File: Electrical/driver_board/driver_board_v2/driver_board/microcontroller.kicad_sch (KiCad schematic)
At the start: 24 parts, among them J1 USB_C_Receptacle_USB2.0_14P, J2 Conn_01x04_Pin, SW1 SW_SPDT, SW2 SW_Push, U1 STM32F446RETx, Y1 8Mhz

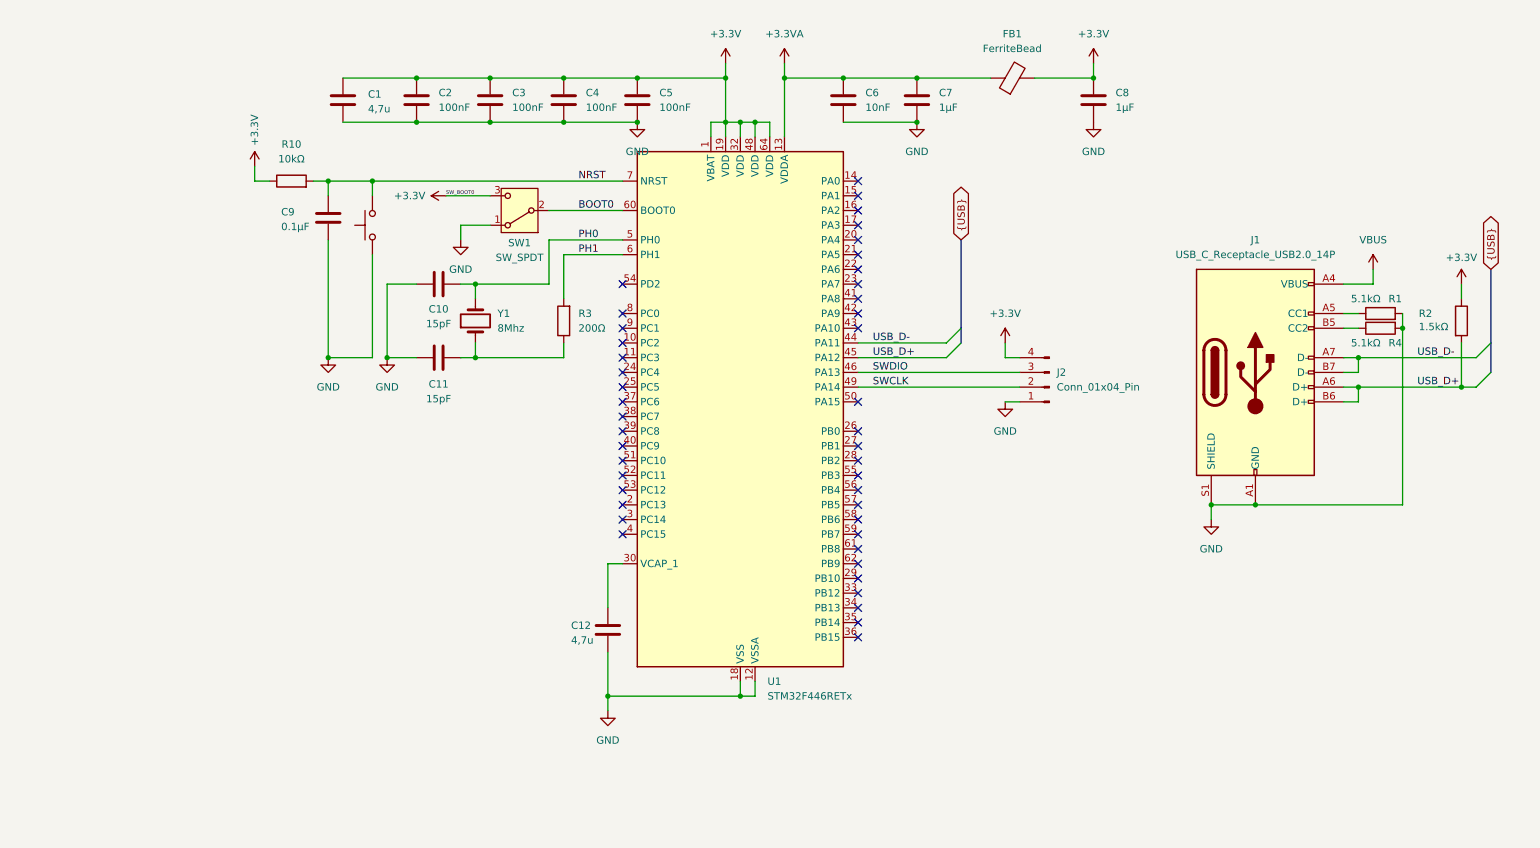
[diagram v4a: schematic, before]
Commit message: Added gripper
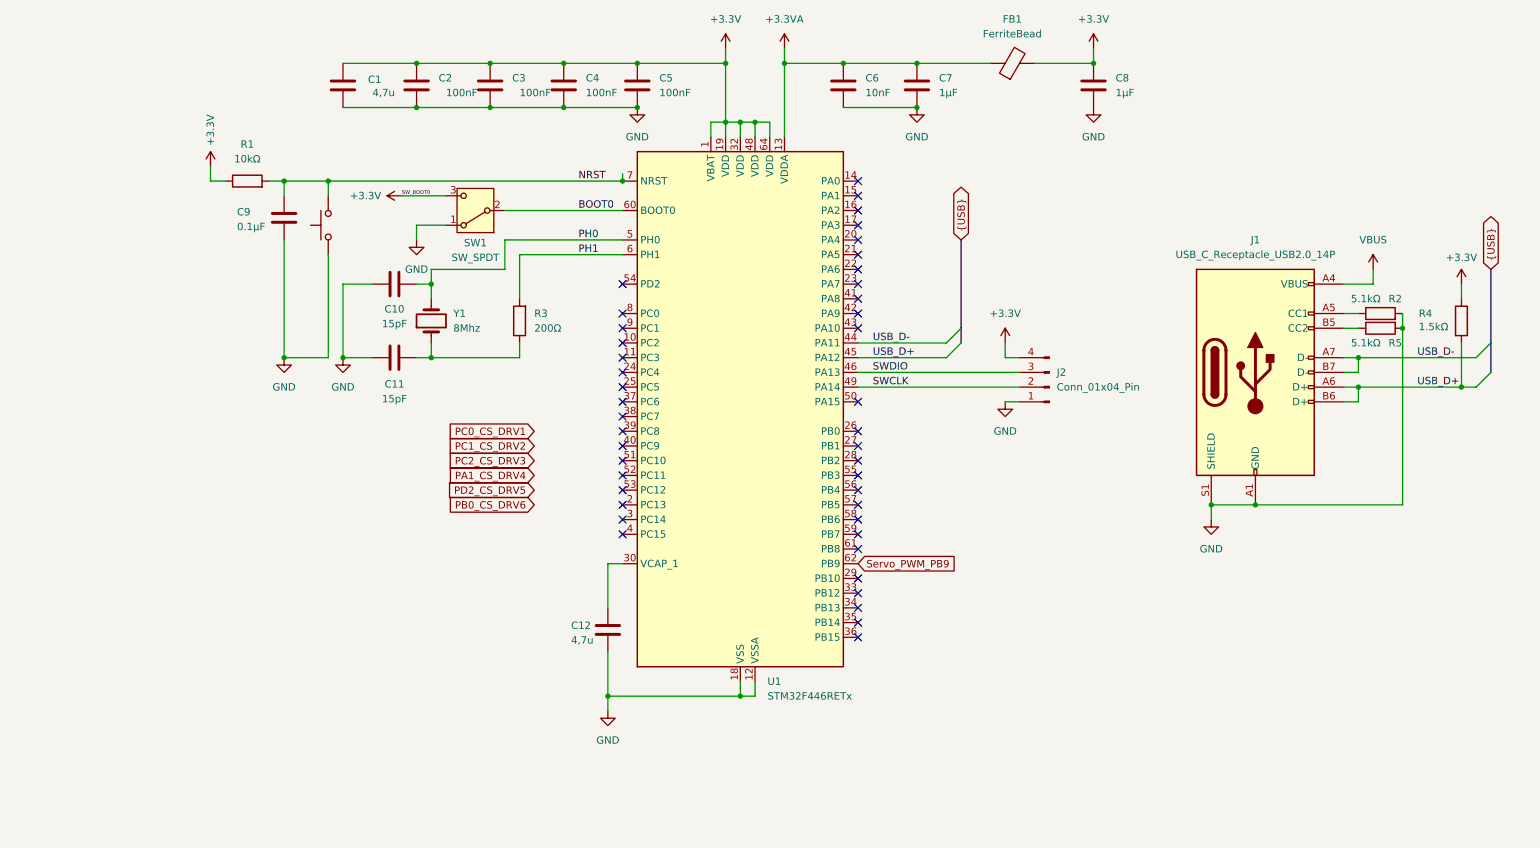
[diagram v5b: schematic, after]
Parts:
- renumbered R10 to R1, R1 to R2, R2 to R4, R4 to R5
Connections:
- net Servo_PWM_PB9: now reaches U1.62 (PB9)
- no-connect marks 44 -> 43
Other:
- moved on the sheet: C1, C10, C11, C2, C3, C4, C5, C6, C7, C8, C9, FB1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

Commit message: Added TMC and MCU Labeling
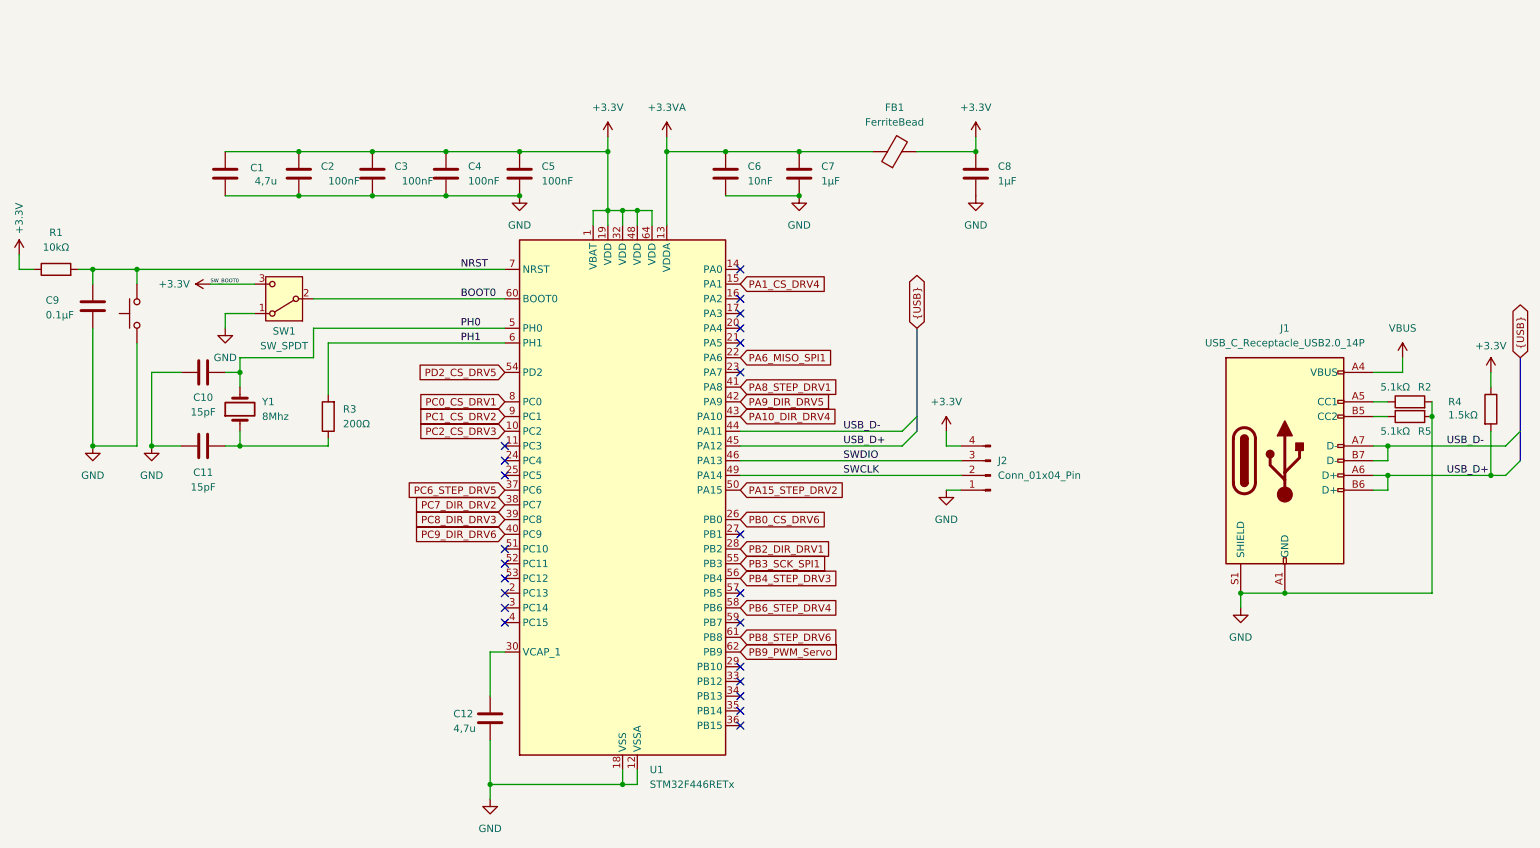
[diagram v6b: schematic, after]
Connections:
- net PA1_CS_DRV4: now also U1.15 (PA1)
- net PB0_CS_DRV6: now also U1.26 (PB0)
- net PC0_CS_DRV1: now also U1.8 (PC0)
- net PC1_CS_DRV2: now also U1.9 (PC1)
- net PC2_CS_DRV3: now also U1.10 (PC2)
- net PD2_CS_DRV5: now also U1.54 (PD2)
- net PA6_MISO_SPI1: now reaches U1.22 (PA6)
- net PB2_DIR_DRV1: now reaches U1.28 (PB2)
- net PC6_STEP_DRV5: now reaches U1.37 (PC6)
- net PC7_DIR_DRV2: now reaches U1.38 (PC7)
- net PC8_DIR_DRV3: now reaches U1.39 (PC8)
- net PC9_DIR_DRV6: now reaches U1.40 (PC9)
- net PA8_STEP_DRV1: now reaches U1.41 (PA8)
- net PA9_DIR_DRV5: now reaches U1.42 (PA9)
- net PA10_DIR_DRV4: now reaches U1.43 (PA10)
- net PA15_STEP_DRV2: now reaches U1.50 (PA15)
- net PB3_SCK_SPI1: now reaches U1.55 (PB3)
- net PB4_STEP_DRV3: now reaches U1.56 (PB4)
- net PB6_STEP_DRV4: now reaches U1.58 (PB6)
- net PB8_STEP_DRV6: now reaches U1.61 (PB8)
- net Servo_PWM_PB9 renamed PB9_PWM_Servo
- no-connect marks 43 -> 23
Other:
- moved on the sheet: C1, C10, C11, C12, C2, C3, C4, C5, C6, C7, C8, C9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

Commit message: Finished TMC Labeling
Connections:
- net PB5_MOSI_SPI1: now reaches U1.57 (PB5)
- no-connect marks 23 -> 22
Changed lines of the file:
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@@
-	)
-	(no_connect
-		(at 147.32 119.38)
 	)
 	(no_connect
@@
 			(effects
 				(font
+					(size 1.27 1.27)
+				)
+				(justify left)
+				(hide yes)
+			)
+		)
+	)
+	(global_label "PB5_MOSI_SPI1"
+		(shape input)
+		(at 147.32 119.38 0)
+		(fields_autoplaced yes)
+		(effects
+			(font
+				(size 1.27 1.27)
+			)
+			(justify left)
+		)
+		(property "Intersheetrefs" "${INTERSHEET_REFS}"
+			(at 164.8799 119.38 0)
+			(effects
+				(font
